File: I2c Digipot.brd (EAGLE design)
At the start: 36.5 x 17.8 mm, 10 parts, among them U1 MAX5387

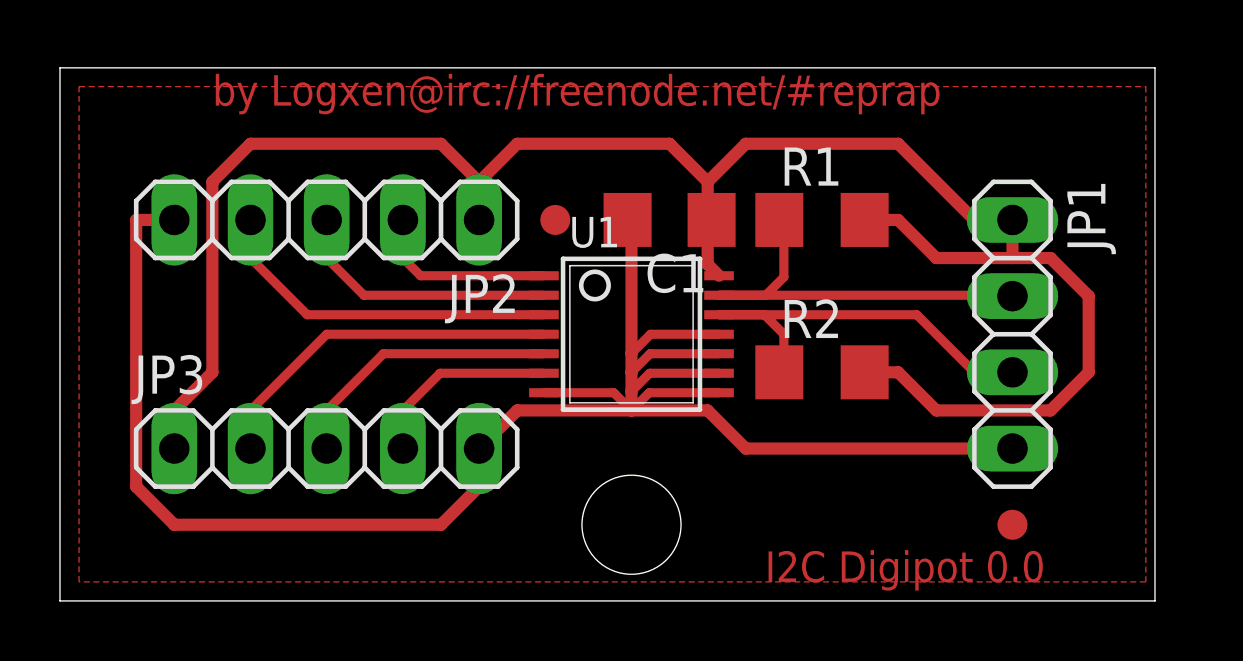
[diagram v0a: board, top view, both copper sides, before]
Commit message: Rotated i2c pull-up resistors to save 0.1" in y
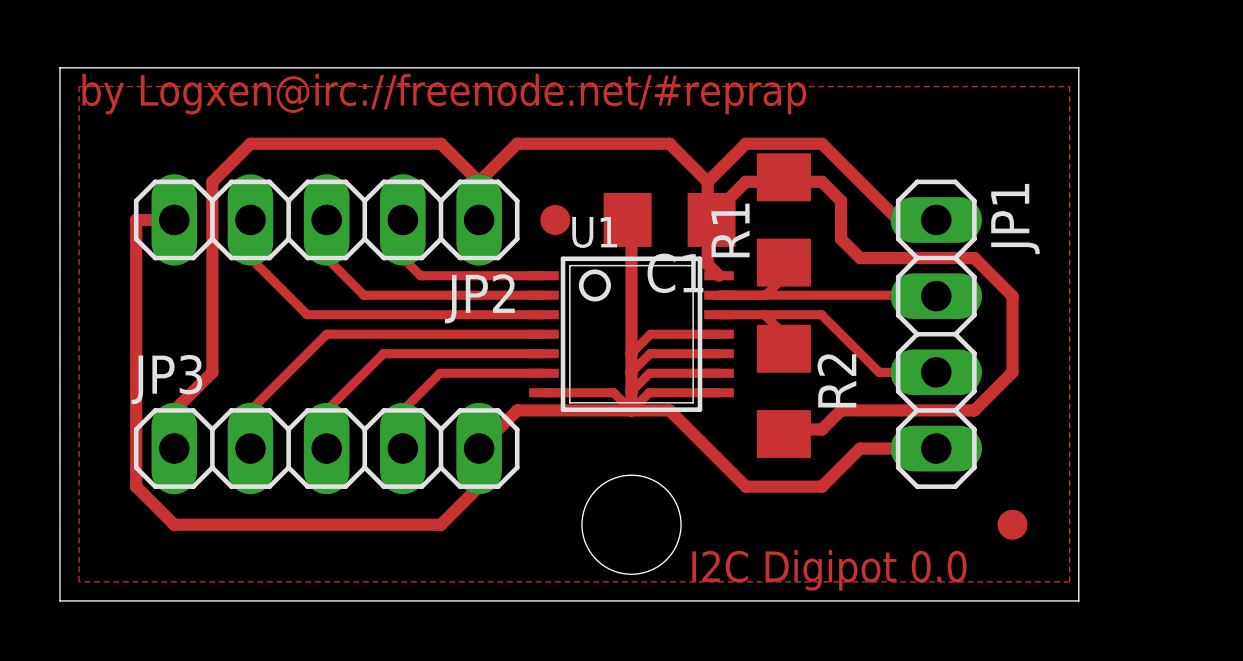
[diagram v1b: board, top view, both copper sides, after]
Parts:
- moved JP1 2.54 mm to (29.2, 8.89)
- moved R2 1.42 mm to (24.1, 6.99), turned to 270 degrees
- moved R1 1.27 mm to (24.1, 12.7), turned to 90 degrees
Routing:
- net SDA: track 14.4 -> 9.44 mm
- net SCL: track 14.3 -> 10.2 mm
- net VCC: track 65.3 -> 67.0 mm
- net GND: track 65.1 -> 63.6 mm
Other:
- board size 36.5 x 17.8 mm -> 34 x 17.8 mm
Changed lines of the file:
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@@
 <layer number="21" name="tPlace" color="7" fill="1" visible="yes" active="yes"/>
 <layer number="22" name="bPlace" color="7" fill="1" visible="yes" active="yes"/>
-<layer number="23" name="tOrigins" color="15" fill="1" visible="no" active="yes"/>
-<layer number="24" name="bOrigins" color="15" fill="1" visible="no" active="yes"/>
+<layer number="23" name="tOrigins" color="15" fill="1" visible="yes" active="yes"/>
+<layer number="24" name="bOrigins" color="15" fill="1" visible="yes" active="yes"/>
 <layer number="25" name="tNames" color="7" fill="1" visible="yes" active="yes"/>
 <layer number="26" name="bNames" color="7" fill="1" visible="yes" active="yes"/>
@@
 <board>
 <plain>
-<wire x1="0" y1="0" x2="36.5" y2="0" width="0" layer="20"/>
-<wire x1="36.5" y1="0" x2="36.5" y2="17.77" width="0" layer="20"/>
-<wire x1="36.5" y1="17.77" x2="0" y2="17.77" width="0" layer="20"/>
+<wire x1="0" y1="0" x2="33.96" y2="0" width="0" layer="20"/>
+<wire x1="33.96" y1="0" x2="33.96" y2="17.77" width="0" layer="20"/>
+<wire x1="33.96" y1="17.77" x2="0" y2="17.77" width="0" layer="20"/>
 <wire x1="0" y1="17.77" x2="0" y2="0" width="0" layer="20"/>
-<text x="23.495" y="0.635" size="1.016" layer="1">I2C Digipot 0.0</text>
-<text x="5.08" y="16.51" size="1.016" layer="1">by Logxen@irc://freenode.net/#reprap</text>
+<text x="20.955" y="0.635" size="1.016" layer="1">I2C Digipot 0.0</text>
+<text x="0.635" y="16.51" size="1.016" layer="1">by Logxen@irc://freenode.net/#reprap</text>
 </plain>
 <attributes>
@@
 <element name="U1" library="logxen" package="TSSOP14" value="MAX5387" x="19.05" y="8.89" rot="R270"/>
 <element name="C1" library="resistor" package="C1206" value="0.1uF" x="20.32" y="12.7" rot="R180"/>
-<element name="R1" library="resistor" package="R1206" value="4.7kOhm" x="25.4" y="12.7"/>
-<element name="R2" library="resistor" package="R1206" value="4.7kOhm" x="25.4" y="7.62"/>
-<element name="JP1" library="pinhead" package="1X04" value="I2C" x="31.75" y="8.89" rot="R270"/>
+<element name="R1" library="resistor" package="R1206" value="4.7kOhm" x="24.13" y="12.7" rot="R90"/>
+<element name="R2" library="resistor" package="R1206" value="4.7kOhm" x="24.13" y="6.985" rot="R270"/>
+<element name="JP1" library="pinhead" package="1X04" value="I2C" x="29.21" y="8.89" rot="R270"/>
 <element name="JP2" library="pinhead" package="1X05" value="POT0" x="8.89" y="12.7" rot="R180"/>
 <element name="JP3" library="pinhead" package="1X05" value="POT1" x="8.89" y="5.08"/>
@@
 <contactref element="JP2" pad="1"/>
 <contactref element="JP3" pad="1"/>
-<wire x1="22.86" y1="15.24" x2="21.59" y2="13.97" width="0.4064" layer="1"/>
 <wire x1="21.59" y1="12.7" x2="21.59" y2="11.2178" width="0.4064" layer="1"/>
 <wire x1="21.59" y1="11.2178" x2="21.9678" y2="10.84" width="0.4064" layer="1"/>
-<wire x1="21.59" y1="13.97" x2="21.59" y2="12.7" width="0.4064" layer="1"/>
 <wire x1="21.59" y1="12.7" x2="21.72" y2="12.7" width="0.4064" layer="1"/>
 <wire x1="21.59" y1="13.97" x2="20.32" y2="15.24" width="0.4064" layer="1"/>
@@
 <wire x1="3.81" y1="6.35" x2="3.81" y2="5.08" width="0.4064" layer="1"/>
 <wire x1="5.08" y1="13.97" x2="5.08" y2="7.62" width="0.4064" layer="1"/>
-<wire x1="26.822" y1="7.62" x2="27.94" y2="7.62" width="0.4064" layer="1"/>
-<wire x1="27.94" y1="7.62" x2="29.21" y2="6.35" width="0.4064" layer="1"/>
-<wire x1="29.21" y1="6.35" x2="33.02" y2="6.35" width="0.4064" layer="1"/>
-<wire x1="33.02" y1="6.35" x2="34.29" y2="7.62" width="0.4064" layer="1"/>
-<wire x1="34.29" y1="7.62" x2="34.29" y2="10.16" width="0.4064" layer="1"/>
-<wire x1="34.29" y1="10.16" x2="33.02" y2="11.43" width="0.4064" layer="1"/>
-<wire x1="33.02" y1="11.43" x2="31.75" y2="11.43" width="0.4064" layer="1"/>
-<wire x1="31.75" y1="11.43" x2="29.21" y2="11.43" width="0.4064" layer="1"/>
-<wire x1="29.21" y1="11.43" x2="27.94" y2="12.7" width="0.4064" layer="1"/>
-<wire x1="27.94" y1="12.7" x2="26.822" y2="12.7" width="0.4064" layer="1"/>
-<wire x1="22.86" y1="15.24" x2="27.94" y2="15.24" width="0.4064" layer="1"/>
-<wire x1="27.94" y1="15.24" x2="30.48" y2="12.7" width="0.4064" layer="1"/>
-<wire x1="30.48" y1="12.7" x2="31.75" y2="12.7" width="0.4064" layer="1"/>
-<wire x1="31.75" y1="12.7" x2="31.75" y2="11.43" width="0.4064" layer="1"/>
+<wire x1="26.035" y1="6.35" x2="30.48" y2="6.35" width="0.4064" layer="1"/>
+<wire x1="30.48" y1="6.35" x2="31.75" y2="7.62" width="0.4064" layer="1"/>
+<wire x1="31.75" y1="7.62" x2="31.75" y2="10.16" width="0.4064" layer="1"/>
+<wire x1="31.75" y1="10.16" x2="30.48" y2="11.43" width="0.4064" layer="1"/>
+<wire x1="22.86" y1="15.24" x2="25.4" y2="15.24" width="0.4064" layer="1"/>
+<wire x1="25.4" y1="15.24" x2="27.94" y2="12.7" width="0.4064" layer="1"/>
+<wire x1="27.94" y1="12.7" x2="29.21" y2="12.7" width="0.4064" layer="1"/>
+<wire x1="22.225" y1="13.335" x2="22.225" y2="13.205" width="0.4064" layer="1"/>
+<wire x1="22.225" y1="13.205" x2="21.72" y2="12.7" width="0.4064" layer="1"/>
+<wire x1="22.86" y1="15.24" x2="21.59" y2="13.97" width="0.4064" layer="1"/>
+<wire x1="21.59" y1="13.97" x2="21.59" y2="12.7" width="0.4064" layer="1"/>
+<wire x1="21.59" y1="12.7" x2="22.86" y2="13.97" width="0.4064" layer="1"/>
+<wire x1="22.86" y1="13.97" x2="24.13" y2="13.97" width="0.4064" layer="1"/>
+<wire x1="25.4" y1="13.97" x2="24.13" y2="13.97" width="0.4064" layer="1"/>
+<wire x1="24.13" y1="13.97" x2="24.13" y2="14.122" width="0.4064" layer="1"/>
+<wire x1="26.035" y1="6.35" x2="25.4" y2="5.715" width="0.4064" layer="1"/>
+<wire x1="25.4" y1="5.715" x2="24.13" y2="5.715" width="0.4064" layer="1"/>
+<wire x1="24.13" y1="5.715" x2="24.13" y2="5.563" width="0.4064" layer="1"/>
+<wire x1="25.4" y1="13.97" x2="26.035" y2="13.335" width="0.4064" layer="1"/>
+<wire x1="26.035" y1="13.335" x2="26.035" y2="12.065" width="0.4064" layer="1"/>
+<wire x1="26.035" y1="12.065" x2="26.67" y2="11.43" width="0.4064" layer="1"/>
+<wire x1="26.67" y1="11.43" x2="30.48" y2="11.43" width="0.4064" layer="1"/>
 </signal>
 <signal name="GND">
@@
 <wire x1="19.05" y1="12.7" x2="18.92" y2="12.7" width="0.4064" layer="1"/>
 <wire x1="19.05" y1="6.35" x2="15.24" y2="6.35" width="0.4064" layer="1"/>
-<wire x1="19.05" y1="6.35" x2="21.59" y2="6.35" width="0.4064" layer="1"/>
 <wire x1="13.97" y1="3.81" x2="13.97" y2="5.08" width="0.4064" layer="1"/>
 <wire x1="15.24" y1="6.35" x2="13.97" y2="5.08" width="0.4064" layer="1"/>
-<wire x1="31.75" y1="5.08" x2="22.86" y2="5.08" width="0.4064" layer="1"/>
-<wire x1="22.86" y1="5.08" x2="21.59" y2="6.35" width="0.4064" layer="1"/>
 <wire x1="21.9678" y1="6.94" x2="19.64" y2="6.94" width="0.3048" layer="1"/>
 <wire x1="19.64" y1="6.94" x2="19.05" y2="6.35" width="0.3048" layer="1"/>
@@
 <wire x1="21.9678" y1="8.89" x2="19.685" y2="8.89" width="0.3048" layer="1"/>
 <wire x1="19.685" y1="8.89" x2="19.05" y2="8.255" width="0.3048" layer="1"/>
-<polygon width="0.4064" layer="1" isolate="0.3048">
+<wire x1="16.1322" y1="6.94" x2="18.46" y2="6.94" width="0.3048" layer="1"/>
+<wire x1="18.46" y1="6.94" x2="19.05" y2="6.35" width="0.3048" layer="1"/>
+<wire x1="29.21" y1="5.08" x2="26.67" y2="5.08" width="0.4064" layer="1"/>
+<wire x1="26.67" y1="5.08" x2="25.4" y2="3.81" width="0.4064" layer="1"/>
+<wire x1="25.4" y1="3.81" x2="22.86" y2="3.81" width="0.4064" layer="1"/>
+<wire x1="22.86" y1="3.81" x2="20.32" y2="6.35" width="0.4064" layer="1"/>
+<wire x1="20.32" y1="6.35" x2="19.05" y2="6.35" width="0.4064" layer="1"/>
+<polygon width="0.4064" layer="1" isolate="0.254">
 <vertex x="0.635" y="17.145"/>
-<vertex x="36.195" y="17.145"/>
-<vertex x="36.195" y="0.635"/>
+<vertex x="33.655" y="17.145"/>
+<vertex x="33.655" y="0.635"/>
 <vertex x="0.635" y="0.635"/>
 </polygon>
-<wire x1="16.1322" y1="6.94" x2="18.46" y2="6.94" width="0.3048" layer="1"/>
-<wire x1="18.46" y1="6.94" x2="19.05" y2="6.35" width="0.3048" layer="1"/>
 </signal>
 <signal name="HA">
@@
 <contactref element="R1" pad="1"/>
 <contactref element="JP1" pad="2"/>
-<wire x1="21.9678" y1="10.19" x2="31.72" y2="10.19" width="0.3048" layer="1"/>
-<wire x1="31.72" y1="10.19" x2="31.75" y2="10.16" width="0.3048" layer="1"/>
 <wire x1="21.9678" y1="10.19" x2="23.525" y2="10.19" width="0.3048" layer="1"/>
 <wire x1="23.525" y1="10.19" x2="24.13" y2="10.795" width="0.3048" layer="1"/>
-<wire x1="24.13" y1="10.795" x2="24.13" y2="12.7" width="0.3048" layer="1"/>
-<wire x1="24.13" y1="12.7" x2="23.978" y2="12.7" width="0.3048" layer="1"/>
+<wire x1="24.13" y1="10.795" x2="24.13" y2="11.278" width="0.3048" layer="1"/>
+<wire x1="21.9678" y1="10.19" x2="29.18" y2="10.19" width="0.3048" layer="1"/>
+<wire x1="29.18" y1="10.19" x2="29.21" y2="10.16" width="0.3048" layer="1"/>
 </signal>
 <signal name="SDA">
@@
 <contactref element="R2" pad="1"/>
 <contactref element="JP1" pad="3"/>
-<wire x1="21.9678" y1="9.54" x2="28.56" y2="9.54" width="0.3048" layer="1"/>
-<wire x1="28.56" y1="9.54" x2="30.48" y2="7.62" width="0.3048" layer="1"/>
-<wire x1="30.48" y1="7.62" x2="31.75" y2="7.62" width="0.3048" layer="1"/>
+<wire x1="23.48" y1="9.54" x2="25.385" y2="9.54" width="0.3048" layer="1"/>
+<wire x1="25.385" y1="9.54" x2="27.305" y2="7.62" width="0.3048" layer="1"/>
+<wire x1="27.305" y1="7.62" x2="29.21" y2="7.62" width="0.3048" layer="1"/>
 <wire x1="21.9678" y1="9.54" x2="23.48" y2="9.54" width="0.3048" layer="1"/>
 <wire x1="23.48" y1="9.54" x2="24.13" y2="8.89" width="0.3048" layer="1"/>
-<wire x1="24.13" y1="8.89" x2="24.13" y2="7.62" width="0.3048" layer="1"/>
-<wire x1="24.13" y1="7.62" x2="23.978" y2="7.62" width="0.3048" layer="1"/>
+<wire x1="24.13" y1="8.89" x2="24.13" y2="8.407" width="0.3048" layer="1"/>
 </signal>
 </signals>
+<errors>
+</errors>
 </board>
 </drawing>

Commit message: rotated pot1 output so it matches pot0
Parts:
- turned JP3 to 180 degrees
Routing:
- net VCC: track 67.0 -> 80.0 mm
- net LB: track 6.49 -> 15.7 mm
- net HB: track 12.1 -> 18.2 mm
- net GND: track 63.6 -> 61.9 mm
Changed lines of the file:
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@@
 <element name="JP1" library="pinhead" package="1X04" value="I2C" x="29.21" y="8.89" rot="R270"/>
 <element name="JP2" library="pinhead" package="1X05" value="POT0" x="8.89" y="12.7" rot="R180"/>
-<element name="JP3" library="pinhead" package="1X05" value="POT1" x="8.89" y="5.08"/>
+<element name="JP3" library="pinhead" package="1X05" value="POT1" x="8.89" y="5.08" rot="R180"/>
 <element name="JP5" library="SparkFun" package="STAND-OFF" value="STAND-OFF" x="19.05" y="2.54"/>
 <element name="JP6" library="SparkFun" package="FIDUCIAL-1X2" value="FIDUCIAL1X2" x="31.75" y="2.54"/>
@@
 <wire x1="13.97" y1="13.97" x2="12.7" y2="15.24" width="0.4064" layer="1"/>
 <wire x1="12.7" y1="15.24" x2="6.35" y2="15.24" width="0.4064" layer="1"/>
-<wire x1="6.35" y1="15.24" x2="5.08" y2="13.97" width="0.4064" layer="1"/>
-<wire x1="5.08" y1="7.62" x2="3.81" y2="6.35" width="0.4064" layer="1"/>
-<wire x1="3.81" y1="6.35" x2="3.81" y2="5.08" width="0.4064" layer="1"/>
-<wire x1="5.08" y1="13.97" x2="5.08" y2="7.62" width="0.4064" layer="1"/>
 <wire x1="26.035" y1="6.35" x2="30.48" y2="6.35" width="0.4064" layer="1"/>
 <wire x1="30.48" y1="6.35" x2="31.75" y2="7.62" width="0.4064" layer="1"/>
@@
 <wire x1="26.035" y1="12.065" x2="26.67" y2="11.43" width="0.4064" layer="1"/>
 <wire x1="26.67" y1="11.43" x2="30.48" y2="11.43" width="0.4064" layer="1"/>
+<wire x1="13.97" y1="5.08" x2="13.97" y2="3.81" width="0.4064" layer="1"/>
+<wire x1="13.97" y1="3.81" x2="11.43" y2="1.27" width="0.4064" layer="1"/>
+<wire x1="11.43" y1="1.27" x2="7.62" y2="1.27" width="0.4064" layer="1"/>
+<wire x1="7.62" y1="1.27" x2="5.08" y2="3.81" width="0.4064" layer="1"/>
+<wire x1="5.08" y1="3.81" x2="5.08" y2="13.97" width="0.4064" layer="1"/>
+<wire x1="5.08" y1="13.97" x2="6.35" y2="15.24" width="0.4064" layer="1"/>
 </signal>
 <signal name="GND">
@@
 <contactref element="JP1" pad="4"/>
 <contactref element="C1" pad="2"/>
-<wire x1="13.97" y1="3.81" x2="12.7" y2="2.54" width="0.4064" layer="1"/>
-<wire x1="12.7" y1="2.54" x2="3.81" y2="2.54" width="0.4064" layer="1"/>
-<wire x1="3.81" y1="2.54" x2="2.54" y2="3.81" width="0.4064" layer="1"/>
-<wire x1="2.54" y1="3.81" x2="2.54" y2="12.7" width="0.4064" layer="1"/>
-<wire x1="2.54" y1="12.7" x2="3.81" y2="12.7" width="0.4064" layer="1"/>
 <wire x1="19.05" y1="6.35" x2="19.05" y2="6.985" width="0.4064" layer="1"/>
 <wire x1="19.05" y1="6.985" x2="19.05" y2="7.62" width="0.4064" layer="1"/>
@@
 <wire x1="19.05" y1="8.255" x2="19.05" y2="12.7" width="0.4064" layer="1"/>
 <wire x1="19.05" y1="12.7" x2="18.92" y2="12.7" width="0.4064" layer="1"/>
-<wire x1="19.05" y1="6.35" x2="15.24" y2="6.35" width="0.4064" layer="1"/>
-<wire x1="13.97" y1="3.81" x2="13.97" y2="5.08" width="0.4064" layer="1"/>
-<wire x1="15.24" y1="6.35" x2="13.97" y2="5.08" width="0.4064" layer="1"/>
 <wire x1="21.9678" y1="6.94" x2="19.64" y2="6.94" width="0.3048" layer="1"/>
 <wire x1="19.64" y1="6.94" x2="19.05" y2="6.35" width="0.3048" layer="1"/>
@@
 <wire x1="22.86" y1="3.81" x2="20.32" y2="6.35" width="0.4064" layer="1"/>
 <wire x1="20.32" y1="6.35" x2="19.05" y2="6.35" width="0.4064" layer="1"/>
+<wire x1="3.81" y1="5.08" x2="3.81" y2="12.7" width="0.4064" layer="1"/>
+<wire x1="3.81" y1="5.08" x2="3.81" y2="3.81" width="0.4064" layer="1"/>
+<wire x1="3.81" y1="3.81" x2="6.985" y2="0.635" width="0.4064" layer="1"/>
+<wire x1="6.985" y1="0.635" x2="12.065" y2="0.635" width="0.4064" layer="1"/>
+<wire x1="12.065" y1="0.635" x2="17.78" y2="6.35" width="0.4064" layer="1"/>
+<wire x1="17.78" y1="6.35" x2="19.05" y2="6.35" width="0.4064" layer="1"/>
 <polygon width="0.4064" layer="1" isolate="0.254">
 <vertex x="0.635" y="17.145"/>
@@
 <contactref element="U1" pad="4"/>
 <contactref element="JP3" pad="2"/>
-<wire x1="16.1322" y1="8.89" x2="8.89" y2="8.89" width="0.3048" layer="1"/>
-<wire x1="8.89" y1="8.89" x2="6.35" y2="6.35" width="0.3048" layer="1"/>
-<wire x1="6.35" y1="6.35" x2="6.35" y2="5.08" width="0.3048" layer="1"/>
+<wire x1="16.1322" y1="8.89" x2="10.16" y2="8.89" width="0.3048" layer="1"/>
+<wire x1="10.16" y1="8.89" x2="7.62" y2="6.35" width="0.3048" layer="1"/>
+<wire x1="7.62" y1="6.35" x2="7.62" y2="3.81" width="0.3048" layer="1"/>
+<wire x1="7.62" y1="3.81" x2="8.89" y2="2.54" width="0.3048" layer="1"/>
+<wire x1="8.89" y1="2.54" x2="10.16" y2="2.54" width="0.3048" layer="1"/>
+<wire x1="10.16" y1="2.54" x2="11.43" y2="3.81" width="0.3048" layer="1"/>
+<wire x1="11.43" y1="3.81" x2="11.43" y2="5.08" width="0.3048" layer="1"/>
 </signal>
 <signal name="WB">
@@
 <contactref element="U1" pad="6"/>
 <contactref element="JP3" pad="4"/>
-<wire x1="16.1322" y1="7.59" x2="12.67" y2="7.59" width="0.3048" layer="1"/>
-<wire x1="12.67" y1="7.59" x2="11.43" y2="6.35" width="0.3048" layer="1"/>
-<wire x1="11.43" y1="6.35" x2="11.43" y2="5.08" width="0.3048" layer="1"/>
+<wire x1="16.1322" y1="7.59" x2="13.94" y2="7.59" width="0.3048" layer="1"/>
+<wire x1="13.94" y1="7.59" x2="12.7" y2="6.35" width="0.3048" layer="1"/>
+<wire x1="12.7" y1="6.35" x2="12.7" y2="3.81" width="0.3048" layer="1"/>
+<wire x1="12.7" y1="3.81" x2="10.795" y2="1.905" width="0.3048" layer="1"/>
+<wire x1="10.795" y1="1.905" x2="8.255" y2="1.905" width="0.3048" layer="1"/>
+<wire x1="8.255" y1="1.905" x2="6.35" y2="3.81" width="0.3048" layer="1"/>
+<wire x1="6.35" y1="3.81" x2="6.35" y2="5.08" width="0.3048" layer="1"/>
 </signal>
 <signal name="SCL">

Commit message: made text thicker
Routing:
- net VCC: track 80.0 -> 81.2 mm
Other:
- board text added: "by Logxen irc://freenode.net/#reprap"
- board text removed: "by Logxen@irc://freenode.net/#reprap"
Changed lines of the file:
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@@
 <wire x1="33.96" y1="17.77" x2="0" y2="17.77" width="0" layer="20"/>
 <wire x1="0" y1="17.77" x2="0" y2="0" width="0" layer="20"/>
-<text x="20.955" y="0.635" size="1.016" layer="1">I2C Digipot 0.0</text>
-<text x="0.635" y="16.51" size="1.016" layer="1">by Logxen@irc://freenode.net/#reprap</text>
+<text x="20.955" y="0.635" size="1.016" layer="1" font="vector" ratio="25">I2C Digipot 0.0</text>
+<text x="0.635" y="16.51" size="1.016" layer="1" font="vector" ratio="25">by Logxen   irc://freenode.net/#reprap</text>
 </plain>
 <attributes>
@@
 <wire x1="21.59" y1="12.7" x2="22.86" y2="13.97" width="0.4064" layer="1"/>
 <wire x1="22.86" y1="13.97" x2="24.13" y2="13.97" width="0.4064" layer="1"/>
-<wire x1="25.4" y1="13.97" x2="24.13" y2="13.97" width="0.4064" layer="1"/>
 <wire x1="24.13" y1="13.97" x2="24.13" y2="14.122" width="0.4064" layer="1"/>
 <wire x1="26.035" y1="6.35" x2="25.4" y2="5.715" width="0.4064" layer="1"/>
 <wire x1="25.4" y1="5.715" x2="24.13" y2="5.715" width="0.4064" layer="1"/>
 <wire x1="24.13" y1="5.715" x2="24.13" y2="5.563" width="0.4064" layer="1"/>
-<wire x1="25.4" y1="13.97" x2="26.035" y2="13.335" width="0.4064" layer="1"/>
-<wire x1="26.035" y1="13.335" x2="26.035" y2="12.065" width="0.4064" layer="1"/>
-<wire x1="26.035" y1="12.065" x2="26.67" y2="11.43" width="0.4064" layer="1"/>
 <wire x1="26.67" y1="11.43" x2="30.48" y2="11.43" width="0.4064" layer="1"/>
 <wire x1="13.97" y1="5.08" x2="13.97" y2="3.81" width="0.4064" layer="1"/>
@@
 <wire x1="5.08" y1="3.81" x2="5.08" y2="13.97" width="0.4064" layer="1"/>
 <wire x1="5.08" y1="13.97" x2="6.35" y2="15.24" width="0.4064" layer="1"/>
+<wire x1="26.67" y1="11.43" x2="25.4" y2="12.7" width="0.4064" layer="1"/>
+<wire x1="25.4" y1="12.7" x2="21.72" y2="12.7" width="0.4064" layer="1"/>
 </signal>
 <signal name="GND">
